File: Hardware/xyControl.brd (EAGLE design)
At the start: 160 x 100 mm, 76 parts, among them IC1 ATMEGA2560-16AU, IC2 74HC573D, IC3 K6X4008C1FSMD, IC4 FT232RL, IC5 74AHC125, Q7 16M, T1 0-XYTHOBUZ_TASTER

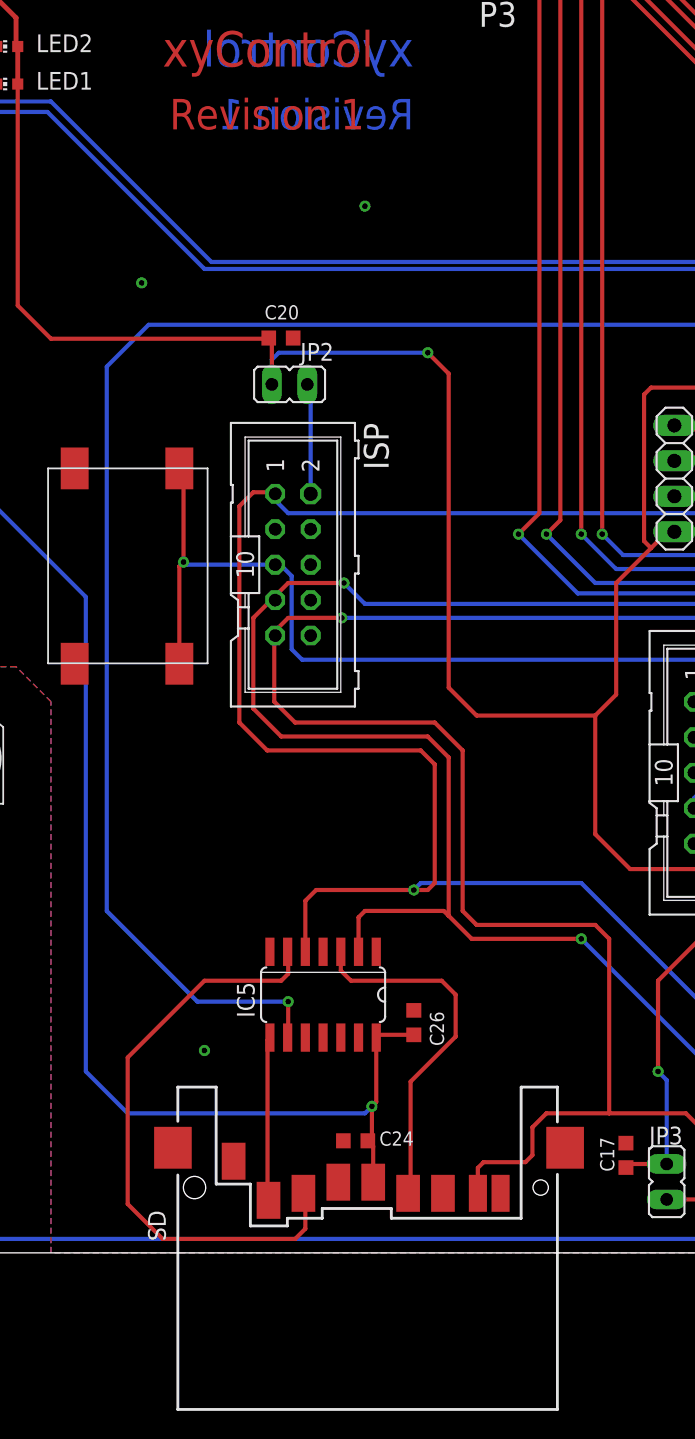
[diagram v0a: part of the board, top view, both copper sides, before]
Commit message: Fixed PCB Layout
SD slot is now rotated correct
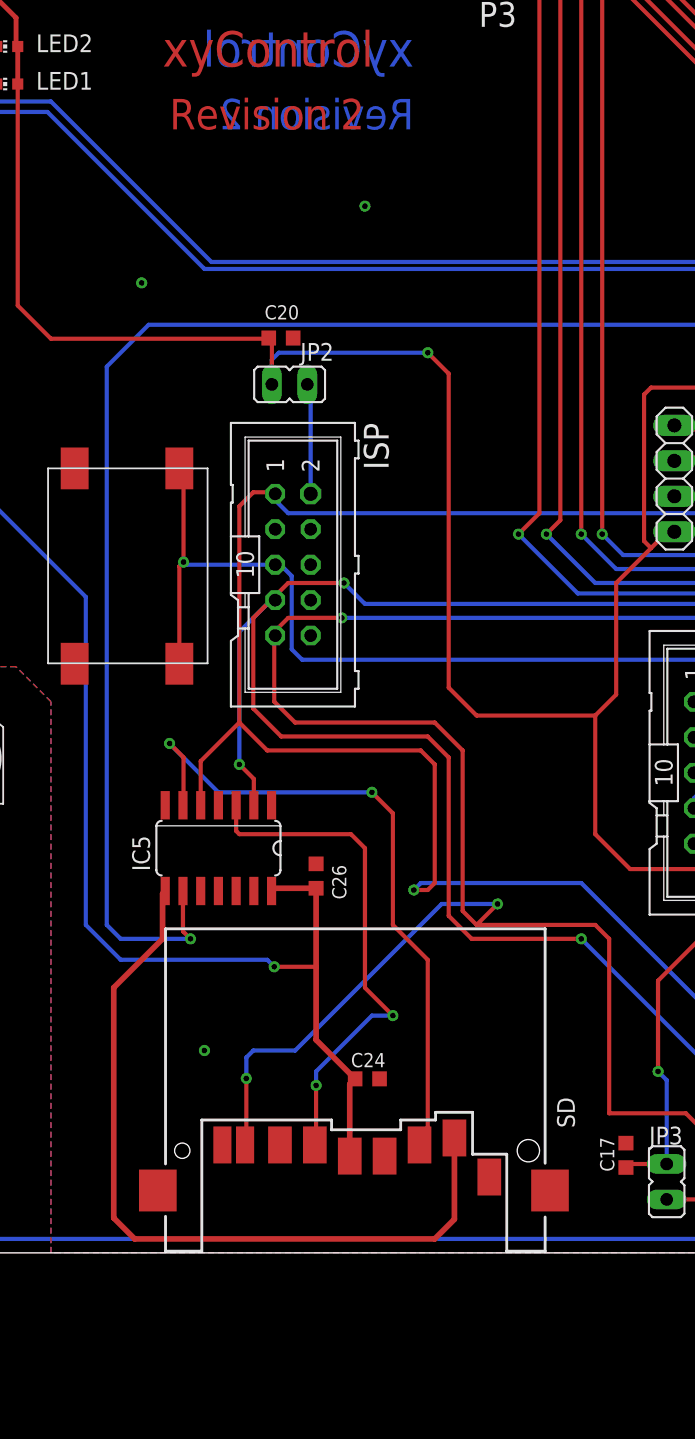
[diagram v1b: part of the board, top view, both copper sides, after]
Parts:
- moved SD 24.1 mm to (69.7, 7.32), turned to 270 degrees
- moved IC5 12.9 mm to (47.5, 29.0)
- moved C26 12.6 mm to (54.5, 27.0)
- moved C24 4.52 mm to (58.2, 12.5), turned to 180 degrees
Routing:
- net N$79: track 11.8 -> 56.4 mm
- net N$38: track 144.9 -> 161.9 mm, vias 2 -> 4
- net N$77: track 25.9 -> 36.9 mm, vias 0 -> 2
- net N$76: track 139.4 -> 132.2 mm
- net N$37: track 138.5 -> 145.6 mm, vias 3 -> 4
- net N$78: track 43.0 -> 48.0 mm, vias 0 -> 2
- net N$39: track 154.0 -> 149.4 mm
- net VDD: track 127.8 -> 123.3 mm
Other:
- board text added: "Revision 2"
- board text removed: "Revision 1"
